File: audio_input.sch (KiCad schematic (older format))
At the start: 22 parts

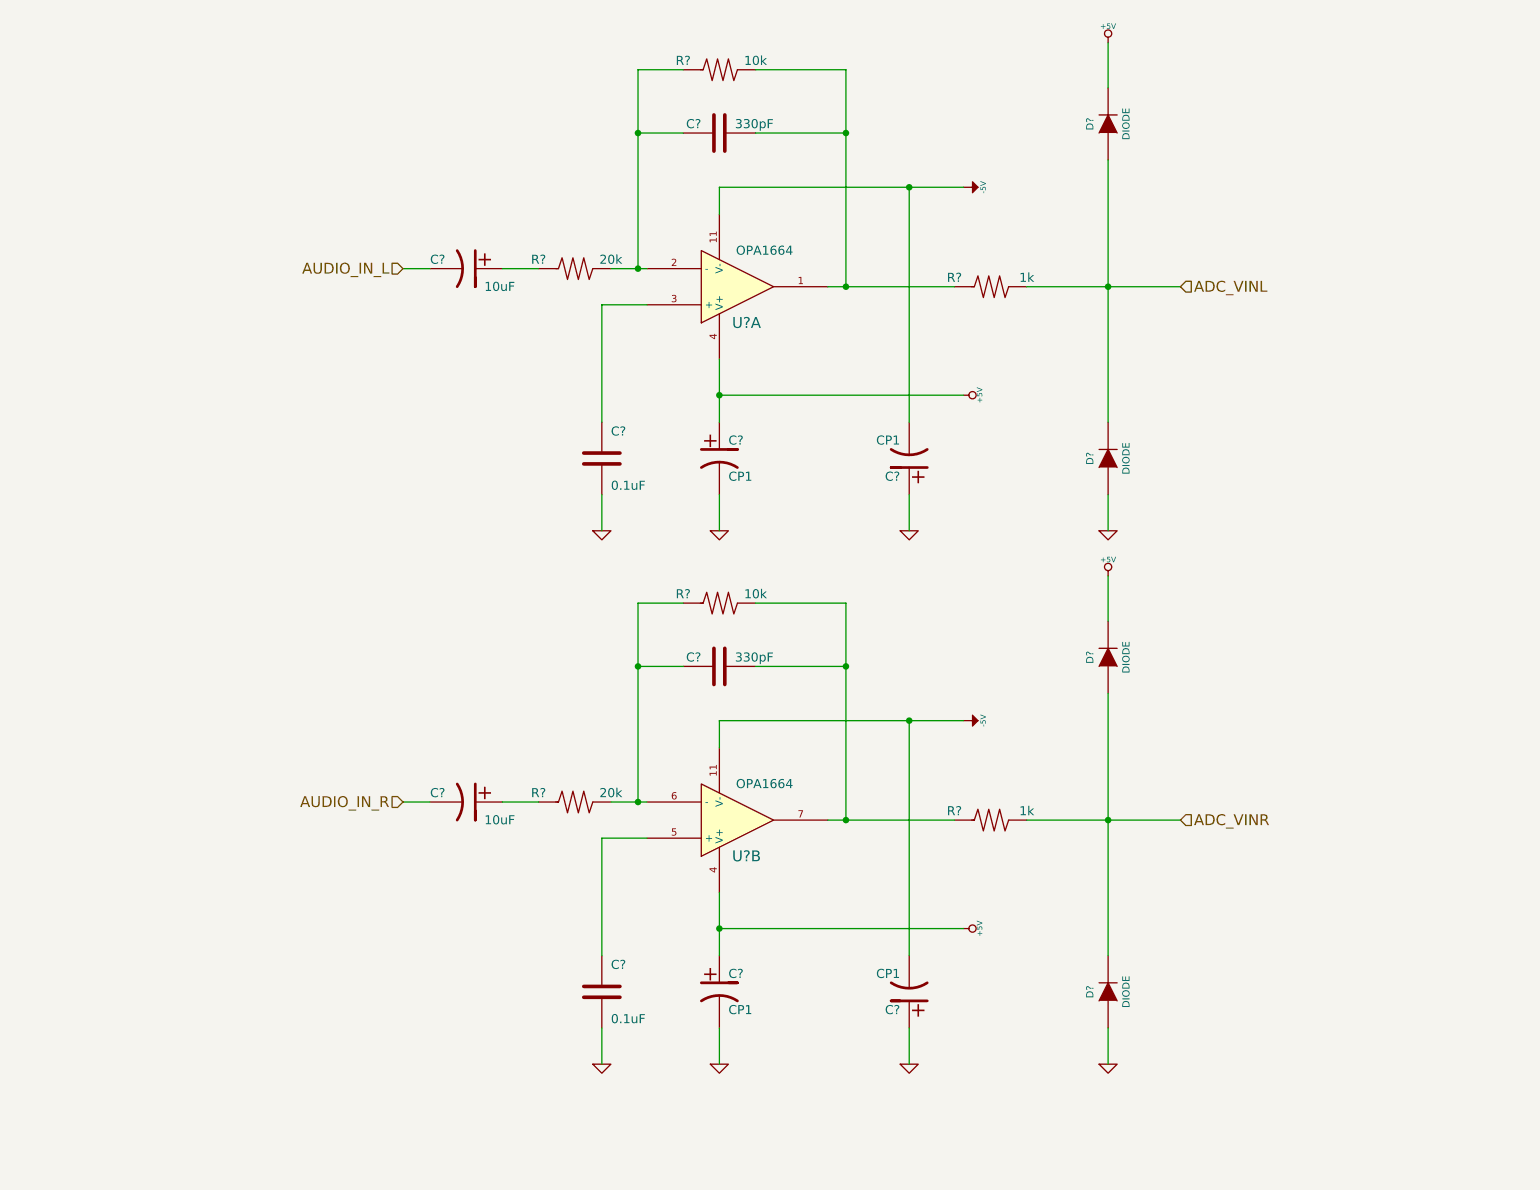
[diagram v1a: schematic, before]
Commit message: Added annotations, fixed ERC errors
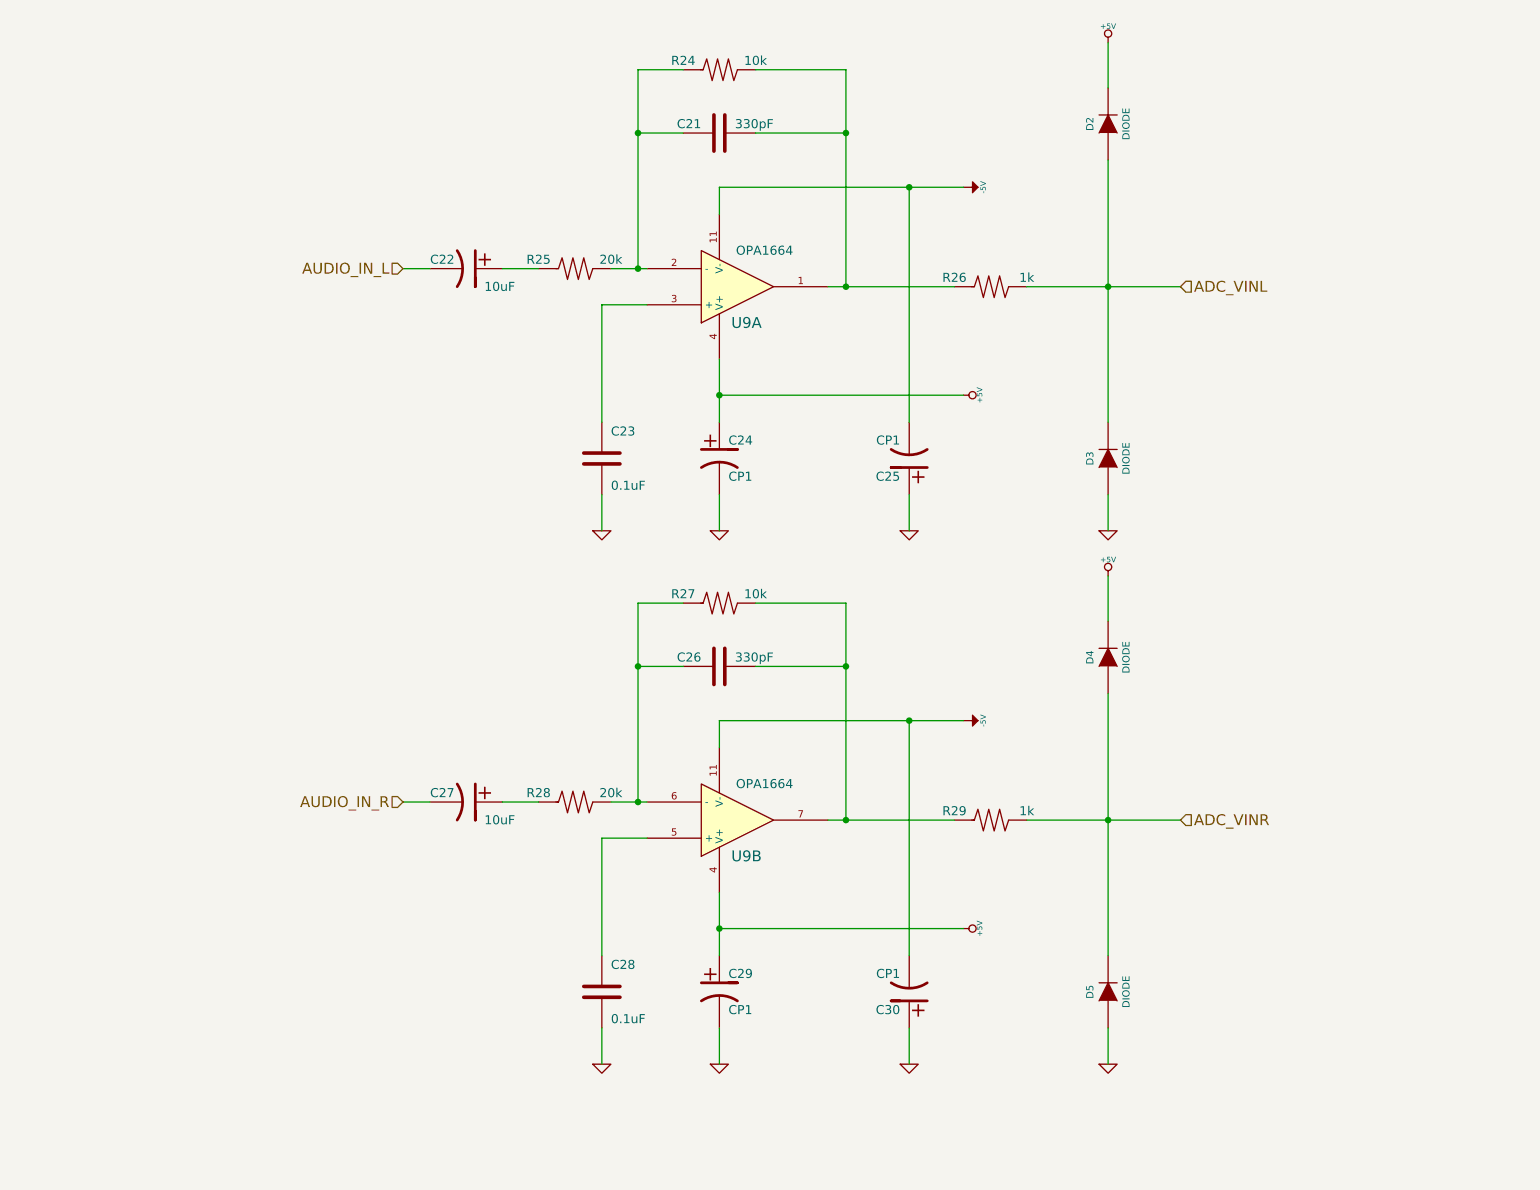
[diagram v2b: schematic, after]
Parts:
- gave numbers to parts that had none: 21

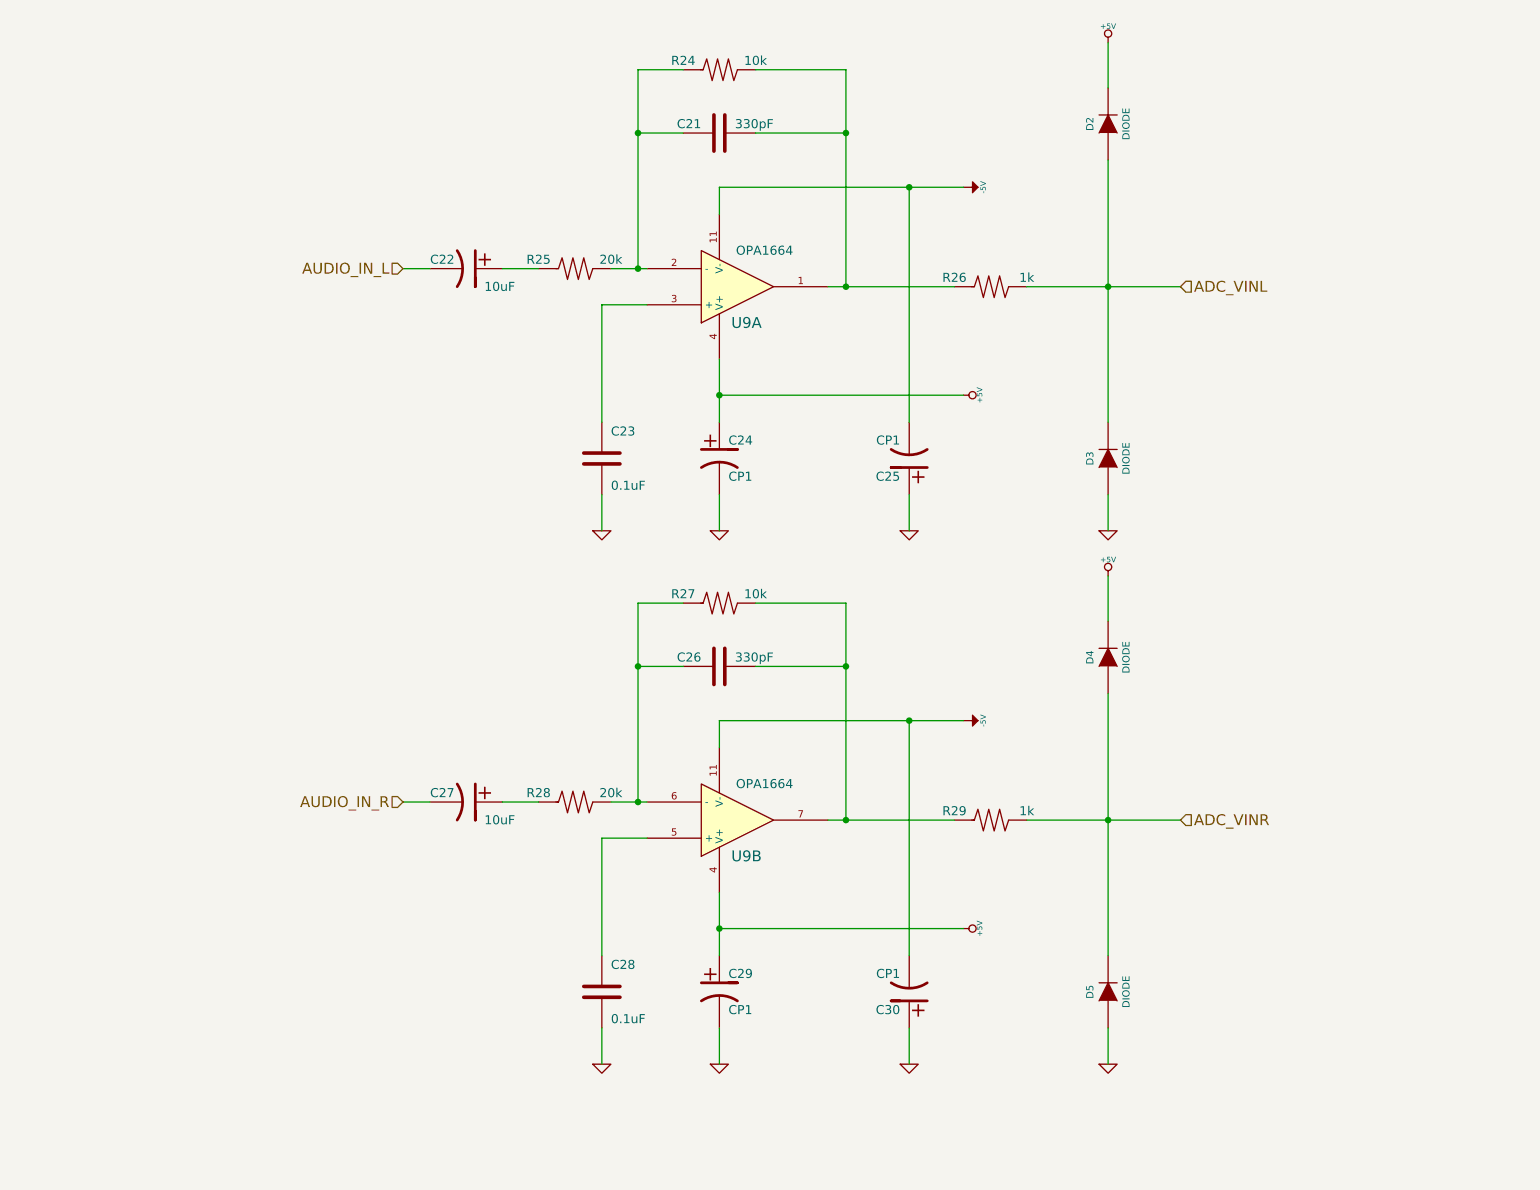
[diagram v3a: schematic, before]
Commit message: Updated decoupling capacitors for op-amp output
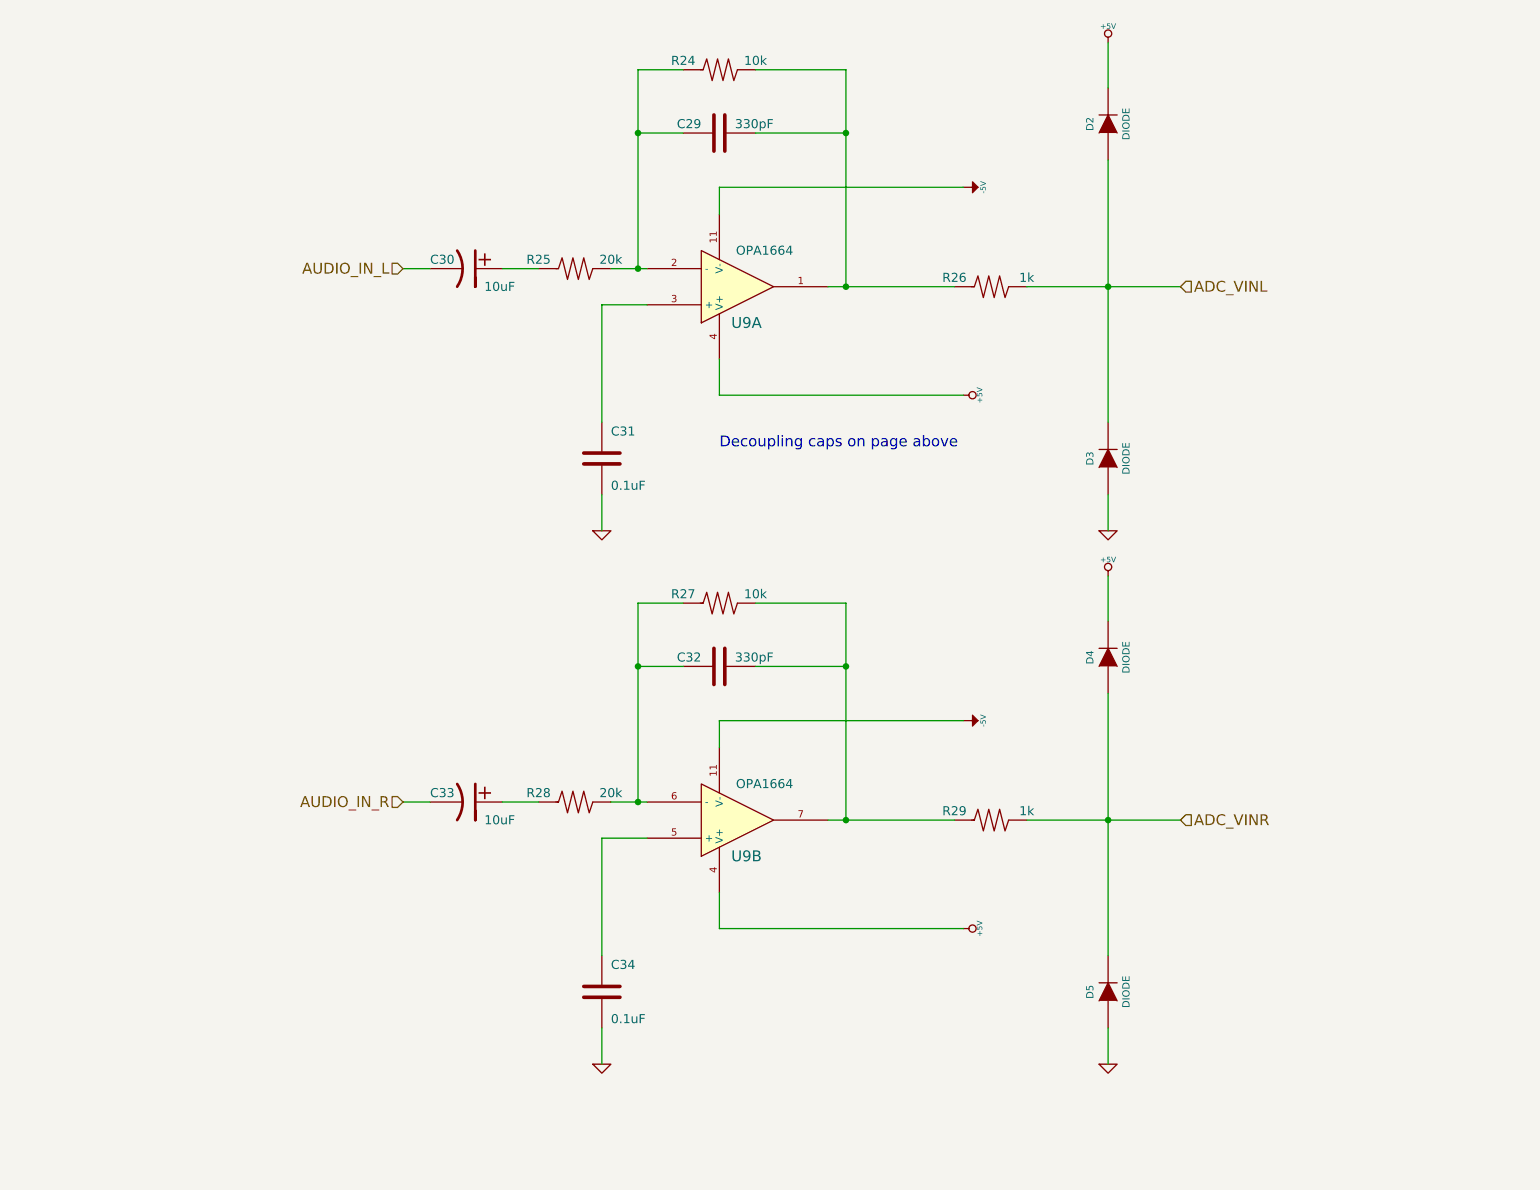
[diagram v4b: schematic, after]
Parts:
- removed C24, C25, C29, C30: CP1, symbol CP1
- renumbered C21 to C29, C22 to C30, C23 to C31, C26 to C32, C27 to C33, C28 to C34
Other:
- note added: "Decoupling caps on page above"
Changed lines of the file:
@@
 	5000 1550 5000 1700
 $Comp
-L -5V #PWR064
+L -5V #PWR075
 U 1 1 5A49B7EA
 P 6350 1550
-F 0 "#PWR064" H 6350 1690 20  0001 C CNN
+F 0 "#PWR075" H 6350 1690 20  0001 C CNN
 F 1 "-5V" H 6350 1660 30  0000 C CNN
 F 2 "" H 6350 1550 60  0000 C CNN
@@
 $EndComp
 $Comp
-L +5V #PWR065
-U 1 1 5A49B806
-P 6350 2700
-F 0 "#PWR065" H 6350 2790 20  0001 C CNN
-F 1 "+5V" H 6350 2790 30  0000 C CNN
-F 2 "" H 6350 2700 60  0000 C CNN
-F 3 "" H 6350 2700 60  0000 C CNN
-	1    6350 2700
-	0    1    1    0
-$EndComp
-Wire Wire Line
-	5000 2500 5000 2850
-$Comp
-L C C21
+L C C29
 U 1 1 5A49B886
 P 5000 1250
-F 0 "C21" V 5050 1350 50  0000 L CNN
+F 0 "C29" V 5050 1350 50  0000 L CNN
 F 1 "330pF" V 5050 950 50  0000 L CNN
 F 2 "" H 5000 1250 60  0000 C CNN
@@
 Connection ~ 4550 2000
 $Comp
-L CP1 C22
+L CP1 C30
 U 1 1 5A49B8DC
 P 3600 2000
-F 0 "C22" V 3550 1800 50  0000 L CNN
+F 0 "C30" V 3550 1800 50  0000 L CNN
 F 1 "10uF" V 3700 2100 50  0000 L CNN
 F 2 "" H 3600 2000 60  0000 C CNN
@@
 $EndComp
 $Comp
-L C C23
+L C C31
 U 1 1 5A49B9EB
 P 4350 3050
-F 0 "C23" H 4400 3200 50  0000 L CNN
+F 0 "C31" H 4400 3200 50  0000 L CNN
 F 1 "0.1uF" H 4400 2900 50  0000 L CNN
 F 2 "" H 4350 3050 60  0000 C CNN
@@
 Wire Wire Line
 	4350 2200 4600 2200
-$Comp
-L CP1 C24
-U 1 1 5A49BB8E
-P 5000 3050
-F 0 "C24" H 5050 3150 50  0000 L CNN
-F 1 "CP1" H 5050 2950 50  0000 L CNN
-F 2 "" H 5000 3050 60  0000 C CNN
-F 3 "" H 5000 3050 60  0000 C CNN
-	1    5000 3050
-	1    0    0    -1
-$EndComp
-Wire Wire Line
-	5000 2700 6350 2700
-Connection ~ 5000 2700
 Wire Wire Line
 	5000 1550 6350 1550
@@
 Connection ~ 5700 1250
 $Comp
-L CP1 C25
-U 1 1 5A49BD05
-P 6050 3050
-F 0 "C25" H 6100 3150 50  0000 L CNN
-F 1 "CP1" H 6100 2950 50  0000 L CNN
-F 2 "" H 6050 3050 60  0000 C CNN
-F 3 "" H 6050 3050 60  0000 C CNN
-	1    6050 3050
-	-1   0    0    1
-$EndComp
-Wire Wire Line
-	6050 2850 6050 1550
-Connection ~ 6050 1550
-$Comp
-L GND #PWR066
+L GND #PWR076
 U 1 1 5A49BD8E
 P 4350 3450
-F 0 "#PWR066" H 4350 3450 30  0001 C CNN
+F 0 "#PWR076" H 4350 3450 30  0001 C CNN
 F 1 "GND" H 4350 3380 30  0001 C CNN
 F 2 "" H 4350 3450 60  0000 C CNN
@@
 Wire Wire Line
 	4350 3450 4350 3250
-$Comp
-L GND #PWR067
-U 1 1 5A49BDF3
-P 5000 3450
-F 0 "#PWR067" H 5000 3450 30  0001 C CNN
-F 1 "GND" H 5000 3380 30  0001 C CNN
-F 2 "" H 5000 3450 60  0000 C CNN
-F 3 "" H 5000 3450 60  0000 C CNN
-	1    5000 3450
-	1    0    0    -1
-$EndComp
-Wire Wire Line
-	5000 3450 5000 3250
-$Comp
-L GND #PWR068
-U 1 1 5A49BE33
-P 6050 3450
-F 0 "#PWR068" H 6050 3450 30  0001 C CNN
-F 1 "GND" H 6050 3380 30  0001 C CNN
-F 2 "" H 6050 3450 60  0000 C CNN
-F 3 "" H 6050 3450 60  0000 C CNN
-	1    6050 3450
-	1    0    0    -1
-$EndComp
-Wire Wire Line
-	6050 3450 6050 3250
 $Comp
 L R R25
@@
 	7150 3450 7150 3250
 $Comp
-L GND #PWR069
+L GND #PWR077
 U 1 1 5A49C264
 P 7150 3450
-F 0 "#PWR069" H 7150 3450 30  0001 C CNN
+F 0 "#PWR077" H 7150 3450 30  0001 C CNN
 F 1 "GND" H 7150 3380 30  0001 C CNN
 F 2 "" H 7150 3450 60  0000 C CNN
@@
 $EndComp
 $Comp
-L +5V #PWR070
+L +5V #PWR078
 U 1 1 5A49C8EC
 P 7150 750
-F 0 "#PWR070" H 7150 840 20  0001 C CNN
+F 0 "#PWR078" H 7150 840 20  0001 C CNN
 F 1 "+5V" H 7150 840 30  0000 C CNN
 F 2 "" H 7150 750 60  0000 C CNN
@@
 	5000 4500 5000 4650
 $Comp
-L -5V #PWR071
+L -5V #PWR079
 U 1 1 5A49EA7F
 P 6350 4500
-F 0 "#PWR071" H 6350 4640 20  0001 C CNN
+F 0 "#PWR079" H 6350 4640 20  0001 C CNN
 F 1 "-5V" H 6350 4610 30  0000 C CNN
 F 2 "" H 6350 4500 60  0000 C CNN
@@
 $EndComp
 $Comp
-L +5V #PWR072
+L +5V #PWR080
 U 1 1 5A49EA85
 P 6350 5650
-F 0 "#PWR072" H 6350 5740 20  0001 C CNN
+F 0 "#PWR080" H 6350 5740 20  0001 C CNN
 F 1 "+5V" H 6350 5740 30  0000 C CNN
 F 2 "" H 6350 5650 60  0000 C CNN
@@
 	0    1    1    0
 $EndComp
-Wire Wire Line
-	5000 5450 5000 5800
-$Comp
-L C C26
+$Comp
+L C C32
 U 1 1 5A49EA8D
 P 5000 4200
-F 0 "C26" V 5050 4300 50  0000 L CNN
+F 0 "C32" V 5050 4300 50  0000 L CNN
 F 1 "330pF" V 5050 3900 50  0000 L CNN
 F 2 "" H 5000 4200 60  0000 C CNN
@@
 Connection ~ 4550 4950
 $Comp
-L CP1 C27
+L CP1 C33
 U 1 1 5A49EA97
 P 3600 4950
-F 0 "C27" V 3550 4750 50  0000 L CNN
+F 0 "C33" V 3550 4750 50  0000 L CNN
 F 1 "10uF" V 3700 5050 50  0000 L CNN
 F 2 "" H 3600 4950 60  0000 C CNN
@@
 $EndComp
 $Comp
-L C C28
+L C C34
 U 1 1 5A49EA9D
 P 4350 6000
-F 0 "C28" H 4400 6150 50  0000 L CNN
+F 0 "C34" H 4400 6150 50  0000 L CNN
 F 1 "0.1uF" H 4400 5850 50  0000 L CNN
 F 2 "" H 4350 6000 60  0000 C CNN
@@
 Wire Wire Line
 	4350 5150 4600 5150
-$Comp
-L CP1 C29
-U 1 1 5A49EAA5
-P 5000 6000
-F 0 "C29" H 5050 6100 50  0000 L CNN
-F 1 "CP1" H 5050 5900 50  0000 L CNN
-F 2 "" H 5000 6000 60  0000 C CNN
-F 3 "" H 5000 6000 60  0000 C CNN
-	1    5000 6000
-	1    0    0    -1
-$EndComp
 Wire Wire Line
 	5000 5650 6350 5650
-Connection ~ 5000 5650
 Wire Wire Line
 	5000 4500 6350 4500
@@
 Connection ~ 5700 4200
 $Comp
-L CP1 C30
-U 1 1 5A49EABE
-P 6050 6000
-F 0 "C30" H 6100 6100 50  0000 L CNN
-F 1 "CP1" H 6100 5900 50  0000 L CNN
-F 2 "" H 6050 6000 60  0000 C CNN
-F 3 "" H 6050 6000 60  0000 C CNN
-	1    6050 6000
-	-1   0    0    1
-$EndComp
-Wire Wire Line
-	6050 5800 6050 4500
-Connection ~ 6050 4500
-$Comp
-L GND #PWR073
+L GND #PWR081
 U 1 1 5A49EAC6
 P 4350 6400
-F 0 "#PWR073" H 4350 6400 30  0001 C CNN
+F 0 "#PWR081" H 4350 6400 30  0001 C CNN
 F 1 "GND" H 4350 6330 30  0001 C CNN
 F 2 "" H 4350 6400 60  0000 C CNN
@@
 Wire Wire Line
 	4350 6400 4350 6200
-$Comp
-L GND #PWR074
-U 1 1 5A49EACE
-P 5000 6400
-F 0 "#PWR074" H 5000 6400 30  0001 C CNN
-F 1 "GND" H 5000 6330 30  0001 C CNN
-F 2 "" H 5000 6400 60  0000 C CNN
-F 3 "" H 5000 6400 60  0000 C CNN
-	1    5000 6400
-	1    0    0    -1
-$EndComp
-Wire Wire Line
-	5000 6400 5000 6200
-$Comp
-L GND #PWR075
-U 1 1 5A49EAD5
-P 6050 6400
-F 0 "#PWR075" H 6050 6400 30  0001 C CNN
-F 1 "GND" H 6050 6330 30  0001 C CNN
-F 2 "" H 6050 6400 60  0000 C CNN
-F 3 "" H 6050 6400 60  0000 C CNN
-	1    6050 6400
-	1    0    0    -1
-$EndComp
-Wire Wire Line
-	6050 6400 6050 6200
 $Comp
 L R R28
@@
 	7150 6400 7150 6200
 $Comp
-L GND #PWR076
+L GND #PWR082
 U 1 1 5A49EAF1
 P 7150 6400
-F 0 "#PWR076" H 7150 6400 30  0001 C CNN
+F 0 "#PWR082" H 7150 6400 30  0001 C CNN
 F 1 "GND" H 7150 6330 30  0001 C CNN
 F 2 "" H 7150 6400 60  0000 C CNN
@@
 $EndComp
 $Comp
-L +5V #PWR077
+L +5V #PWR083
 U 1 1 5A49EB03
 P 7150 3700
-F 0 "#PWR077" H 7150 3790 20  0001 C CNN
+F 0 "#PWR083" H 7150 3790 20  0001 C CNN
 F 1 "+5V" H 7150 3790 30  0000 C CNN
 F 2 "" H 7150 3700 60  0000 C CNN
@@
 Text HLabel 7550 5050 2    60   Input ~ 0
 ADC_VINR
+Text Notes 5000 3000 0    60   ~ 0
+Decoupling caps on page above
+Wire Wire Line
+	5000 2700 6350 2700
+$Comp
+L +5V #PWR084
+U 1 1 5A49B806
+P 6350 2700
+F 0 "#PWR084" H 6350 2790 20  0001 C CNN
+F 1 "+5V" H 6350 2790 30  0000 C CNN
+F 2 "" H 6350 2700 60  0000 C CNN
+F 3 "" H 6350 2700 60  0000 C CNN
+	1    6350 2700
+	0    1    1    0
+$EndComp
+Wire Wire Line
+	5000 2700 5000 2500
+Wire Wire Line
+	5000 5650 5000 5450
 $EndSCHEMATC
